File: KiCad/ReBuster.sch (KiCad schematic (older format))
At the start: 12 parts, among them U3 SN74CBTD16210, U4 SN74LVC16T245DGVR, U5 SN74CBTD16210, U6 SN74CBTD16210, U7 74LVC2G07GV,125, U8 PLCC_84_plug, U9 PLCC_84_plug

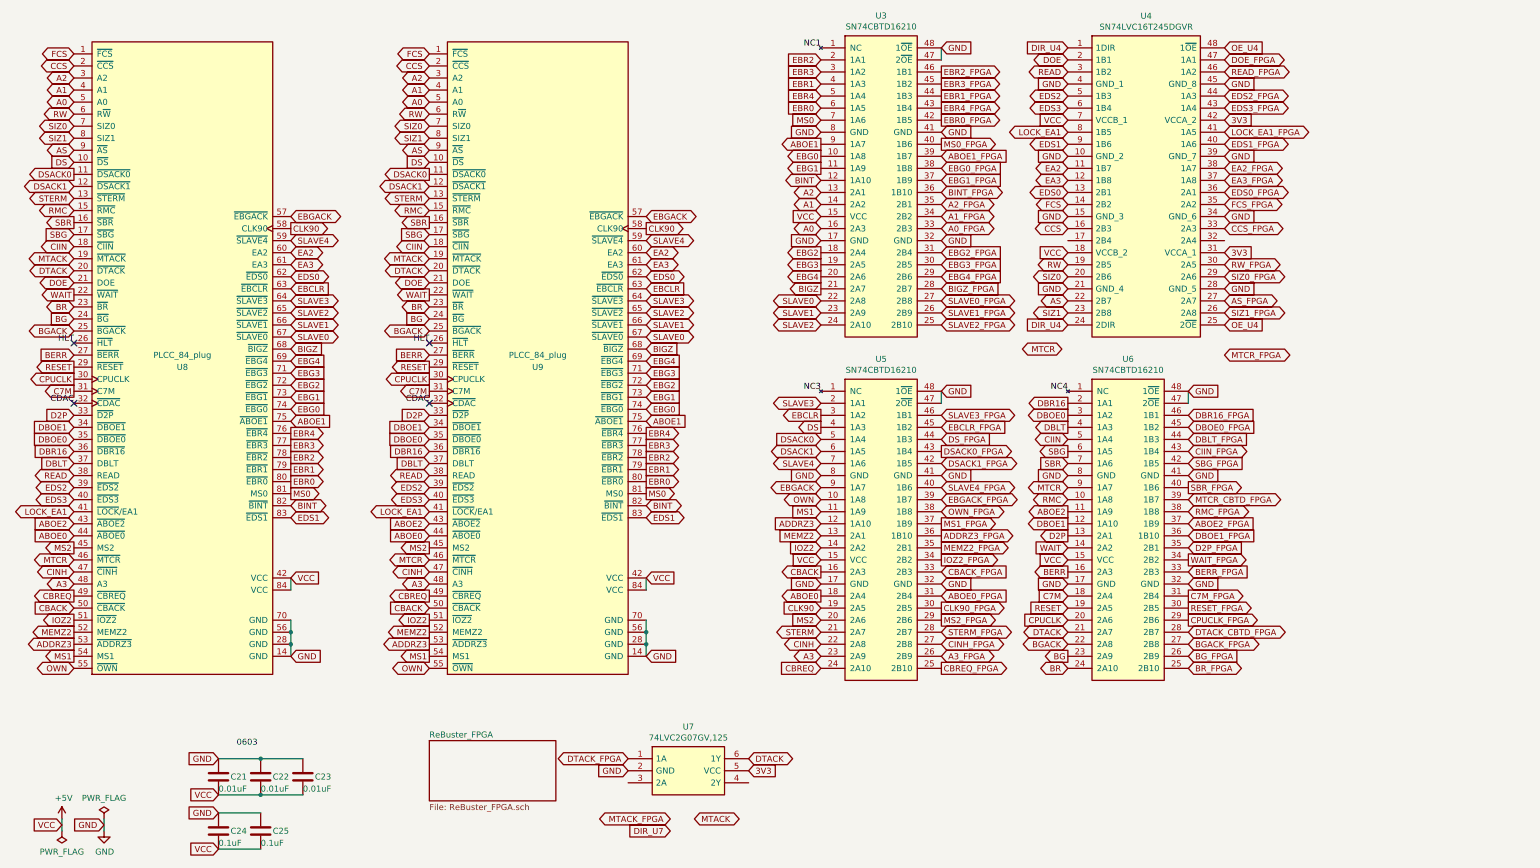
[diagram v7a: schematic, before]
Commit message: Replace SN74LVC16T245DGVR with SN74LVC16245ADGVR and fix caps C24,C25 to instead be connected to 3V3
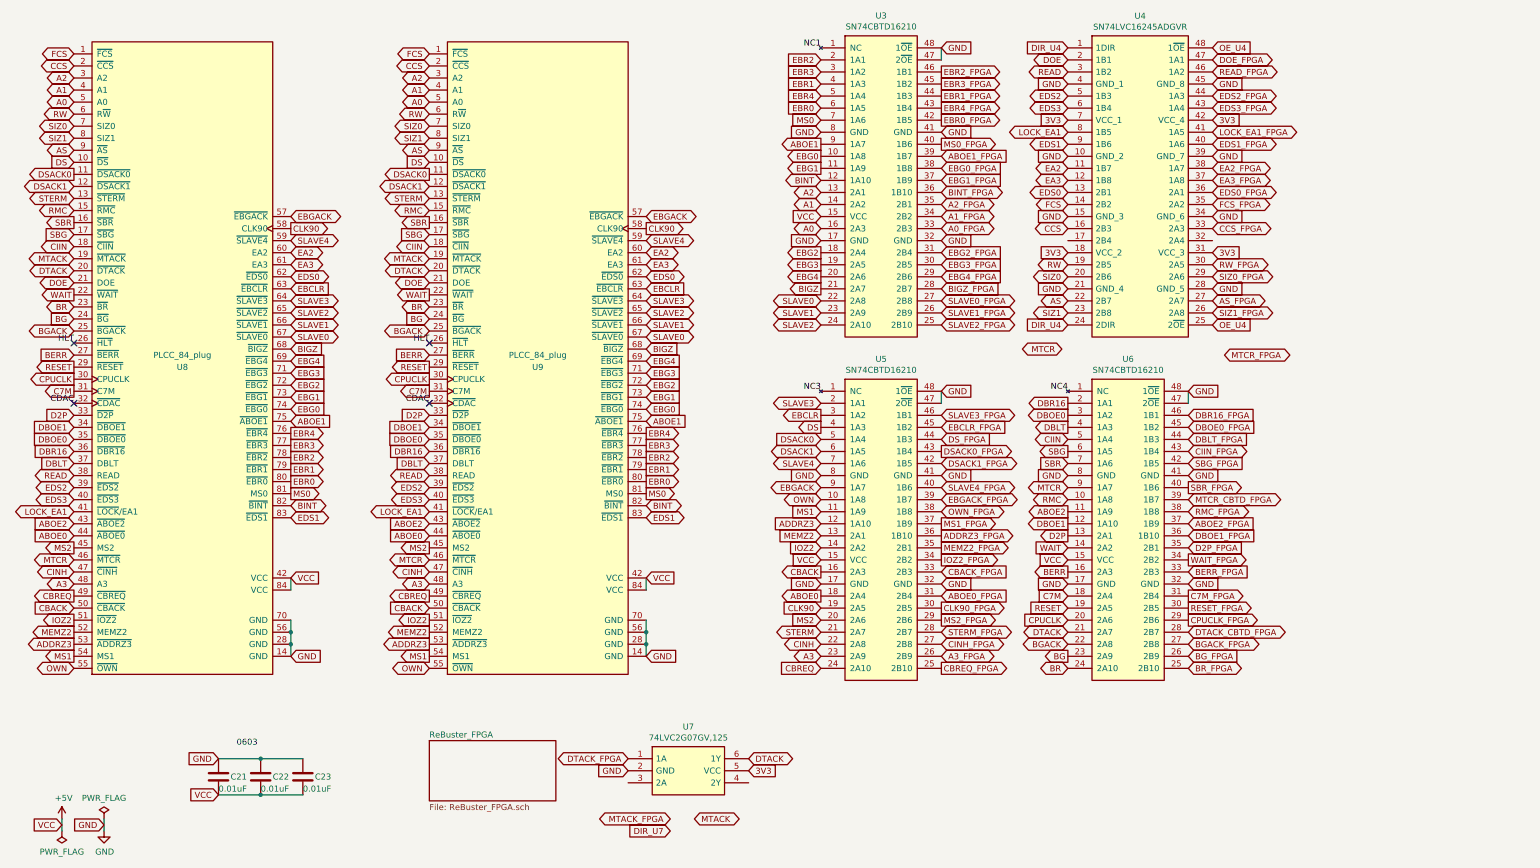
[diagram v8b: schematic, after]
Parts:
- removed C24: 0.1uF, ReBuster:C_0603_1608Metric_Pad1.05x0.95mm_HandSolder_extended, symbol Device:C
- removed C25: 0.1uF, Capacitor_SMD:C_0603_1608Metric_Pad1.05x0.95mm_HandSolder, symbol Device:C
- removed U4: SN74LVC16T245DGVR, Package_SO:TSSOP-48_4.4x9.7mm_P0.4mm, symbol ReBuster:SN74LVC16T245DGVR
- added U4: SN74LVC16245ADGVR, ReBuster:TSSOP-48_4.4x9.7mm_P0.4mm_custom, symbol ReBuster:SN74LVC16245ADGVR
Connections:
- net 3V3: now also U4.18 (VCC_2), U4.31 (VCC_3), U4.42 (VCC_4), U4.7 (VCC_1)
- net AS: now also U4.22 (2B7)
- net AS_FPGA: now also U4.27 (2A7)
- net CCS: now also U4.16 (2B3)
- net CCS_FPGA: now also U4.33 (2A3)
- net DIR_U4: now also U4.1 (1DIR), U4.24 (2DIR)
- net DOE: now also U4.2 (1B1)
- net DOE_FPGA: now also U4.47 (1A1)
- net EA2: now also U4.11 (1B7)
- net EA2_FPGA: now also U4.38 (1A7)
- net EA3: now also U4.12 (1B8)
- net EA3_FPGA: now also U4.37 (1A8)
- net EDS0: now also U4.13 (2B1)
- net EDS0_FPGA: now also U4.36 (2A1)
- net EDS1: now also U4.9 (1B6)
- net EDS1_FPGA: now also U4.40 (1A6)
- net EDS2: now also U4.5 (1B3)
- net EDS2_FPGA: now also U4.44 (1A3)
- net EDS3: now also U4.6 (1B4)
- net EDS3_FPGA: now also U4.43 (1A4)
- net FCS: now also U4.14 (2B2)
- net FCS_FPGA: now also U4.35 (2A2)
- net GND: now also U4.10 (GND_2), U4.15 (GND_3), U4.21 (GND_4), U4.28 (GND_5), U4.34 (GND_6), U4.39 (GND_7), U4.4 (GND_1), U4.45 (GND_8)
- net LOCK_EA1: now also U4.8 (1B5)
- net LOCK_EA1_FPGA: now also U4.41 (1A5)
- net OE_U4: now also U4.25 (2~OE), U4.48 (1~OE)
- net READ: now also U4.3 (1B2)
- net READ_FPGA: now also U4.46 (1A2)
- net RW: now also U4.19 (2B5)
- net RW_FPGA: now also U4.30 (2A5)
- net SIZ0: now also U4.20 (2B6)
- net SIZ0_FPGA: now also U4.29 (2A6)
- net SIZ1: now also U4.23 (2B8)
- net SIZ1_FPGA: now also U4.26 (2A8)
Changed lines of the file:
@@
 Text GLabel 8150 1650 2    50   Input ~ 0
 GND
-Text GLabel 10500 1850 2    50   Input ~ 0
+Text GLabel 10400 1850 2    50   Input ~ 0
 GND
 Text GLabel 9200 1250 0    50   Input ~ 0
 GND
-Text GLabel 10500 1250 2    50   Input ~ 0
+Text GLabel 10400 1250 2    50   Input ~ 0
 GND
 Text GLabel 10200 5400 2    50   Input ~ 0
@@
 Text GLabel 8150 4500 2    50   Input ~ 0
 GND
-Text GLabel 9200 1550 0    50   Input ~ 0
-VCC
 Text GLabel 9200 1850 0    50   Input ~ 0
 GND
@@
 Text GLabel 7150 5200 0    50   Input ~ 0
 VCC
-Text GLabel 10500 3150 2    50   BiDi ~ 0
+Text GLabel 10400 3150 2    50   BiDi ~ 0
 SIZ1_FPGA
 Text GLabel 8150 1450 2    50   Output ~ 0
@@
 Text GLabel 8150 2050 2    50   Input ~ 0
 EBG1_FPGA
-Text GLabel 10500 1750 2    50   BiDi ~ 0
+Text GLabel 10400 1750 2    50   BiDi ~ 0
 EDS1_FPGA
-Text GLabel 10500 2250 2    50   BiDi ~ 0
+Text GLabel 10400 2250 2    50   BiDi ~ 0
 FCS_FPGA
 Text GLabel 8150 2650 2    50   Input ~ 0
@@
 Text GLabel 10200 5200 2    50   Output ~ 0
 WAIT_FPGA
-Text GLabel 10500 1050 2    50   BiDi ~ 0
+Text GLabel 10400 1050 2    50   BiDi ~ 0
 DOE_FPGA
 Text GLabel 5550 6850 0    50   BiDi ~ 0
@@
 Text GLabel 10200 4800 2    50   BiDi ~ 0
 RMC_FPGA
-Text GLabel 10500 2450 2    50   BiDi ~ 0
+Text GLabel 10400 2450 2    50   BiDi ~ 0
 CCS_FPGA
 Text GLabel 8150 2250 2    50   BiDi ~ 0
@@
 Text GLabel 10200 4400 2    50   Input ~ 0
 SBG_FPGA
-Text GLabel 10500 2750 2    50   BiDi ~ 0
+Text GLabel 10400 2750 2    50   BiDi ~ 0
 RW_FPGA
-Text GLabel 10500 2850 2    50   BiDi ~ 0
+Text GLabel 10400 2850 2    50   BiDi ~ 0
 SIZ0_FPGA
 Text GLabel 8150 5800 2    50   BiDi ~ 0
@@
 Text GLabel 8150 4200 2    50   Input ~ 0
 DS_FPGA
-Text GLabel 10500 3050 2    50   BiDi ~ 0
+Text GLabel 10400 3050 2    50   BiDi ~ 0
 AS_FPGA
 Text GLabel 8150 4000 2    50   BiDi ~ 0
@@
 Text GLabel 8150 4100 2    50   Input ~ 0
 EBCLR_FPGA
-Text GLabel 10500 2150 2    50   BiDi ~ 0
+Text GLabel 10400 2150 2    50   BiDi ~ 0
 EDS0_FPGA
-Text GLabel 10500 2050 2    50   BiDi ~ 0
+Text GLabel 10400 2050 2    50   BiDi ~ 0
 EA3_FPGA
-Text GLabel 10500 1950 2    50   BiDi ~ 0
+Text GLabel 10400 1950 2    50   BiDi ~ 0
 EA2_FPGA
 Text GLabel 8150 4700 2    50   BiDi ~ 0
@@
 Text GLabel 10200 4100 2    50   Input ~ 0
 DBOE0_FPGA
-Text GLabel 10500 1150 2    50   BiDi ~ 0
+Text GLabel 10400 1150 2    50   BiDi ~ 0
 READ_FPGA
-Text GLabel 10500 1350 2    50   BiDi ~ 0
+Text GLabel 10400 1350 2    50   BiDi ~ 0
 EDS2_FPGA
-Text GLabel 10500 1450 2    50   BiDi ~ 0
+Text GLabel 10400 1450 2    50   BiDi ~ 0
 EDS3_FPGA
-Text GLabel 10500 1650 2    50   BiDi ~ 0
+Text GLabel 10400 1650 2    50   BiDi ~ 0
 LOCK_EA1_FPGA
 Text GLabel 10200 4900 2    50   Input ~ 0
@@
 F 3 "~" H 2150 7000 50  0001 C CNN
 	1    2150 7000
-	1    0    0    -1
-$EndComp
-$Comp
-L Device:C C25
-U 1 1 605D3E60
-P 2500 7450
-F 0 "C25" H 2600 7450 50  0000 L CNN
-F 1 "0.1uF" H 2500 7350 50  0000 L CNN
-F 2 "Capacitor_SMD:C_0603_1608Metric_Pad1.05x0.95mm_HandSolder" H 2538 7300 50  0001 C CNN
-F 3 "~" H 2500 7450 50  0001 C CNN
-	1    2500 7450
 	1    0    0    -1
 $EndComp
@@
 Text GLabel 8150 4300 2    50   Output ~ 0
 DSACK0_FPGA
-$Comp
-L ReBuster:SN74LVC16T245DGVR U4
-U 1 1 69A5D76D
-P 9850 2100
-F 0 "U4" H 9850 3515 50  0000 C CNN
-F 1 "SN74LVC16T245DGVR" H 9850 3424 50  0000 C CNN
-F 2 "Package_SO:TSSOP-48_4.4x9.7mm_P0.4mm" H 10350 3350 50  0001 L CNN
-F 3 "http://www.ti.com/lit/gpn/sn74lvc16t245" H 10350 3250 50  0001 L CNN
-	1    9850 2100
-	1    0    0    -1
-$EndComp
-Text GLabel 10500 2350 2    50   Input ~ 0
-GND
-Text GLabel 10500 2950 2    50   Input ~ 0
+Text GLabel 10400 2350 2    50   Input ~ 0
+GND
+Text GLabel 10400 2950 2    50   Input ~ 0
 GND
 Text GLabel 9200 2950 0    50   Input ~ 0
@@
 Text GLabel 9200 3250 0    50   Input ~ 0
 DIR_U4
-Text GLabel 10500 950  2    50   Input ~ 0
+Text GLabel 10400 950  2    50   Input ~ 0
 OE_U4
-Text GLabel 10500 3250 2    50   Input ~ 0
+Text GLabel 10400 3250 2    50   Input ~ 0
 OE_U4
-Text GLabel 9200 2650 0    50   Input ~ 0
-VCC
-Text GLabel 10500 1550 2    50   Input ~ 0
+Text GLabel 10400 1550 2    50   Input ~ 0
 3V3
-Text GLabel 10500 2650 2    50   Input ~ 0
+Text GLabel 10400 2650 2    50   Input ~ 0
 3V3
 Text GLabel 6550 6950 2    50   Input ~ 0
@@
 	1    0    0    -1
 $EndComp
-$Comp
-L Device:C C24
-U 1 1 69EC0A34
-P 2150 7450
-F 0 "C24" H 2250 7450 50  0000 L CNN
-F 1 "0.1uF" H 2150 7350 50  0000 L CNN
-F 2 "ReBuster:C_0603_1608Metric_Pad1.05x0.95mm_HandSolder_extended" H 2188 7300 50  0001 C CNN
-F 3 "~" H 2150 7450 50  0001 C CNN
-	1    2150 7450
-	1    0    0    -1
-$EndComp
-Text GLabel 2150 7300 0    50   Input ~ 0
-GND
-Text GLabel 2150 7600 0    50   Input ~ 0
-VCC
-Wire Wire Line
-	2500 7300 2150 7300
-Wire Wire Line
-	2500 7600 2150 7600
 Text Label 3900 3900 2    50   ~ 0
 CDAC
@@
 	1    0    0    -1
 $EndComp
+Text GLabel 9200 2650 0    50   Input ~ 0
+3V3
+Text GLabel 9200 1550 0    50   Input ~ 0
+3V3
+$Comp
+L ReBuster:SN74LVC16245ADGVR U4
+U 1 1 6A051905
+P 9800 2100
+F 0 "U4" H 9800 3515 50  0000 C CNN
+F 1 "SN74LVC16245ADGVR" H 9800 3424 50  0000 C CNN
+F 2 "ReBuster:TSSOP-48_4.4x9.7mm_P0.4mm_custom" H 10250 3350 50  0001 L CNN
+F 3 "http://www.ti.com/lit/gpn/sn74lvc16245a" H 10250 3250 50  0001 L CNN
+	1    9800 2100
+	1    0    0    -1
+$EndComp
